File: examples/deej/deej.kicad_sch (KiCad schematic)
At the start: 27 parts, among them U1 2821, U2 5836

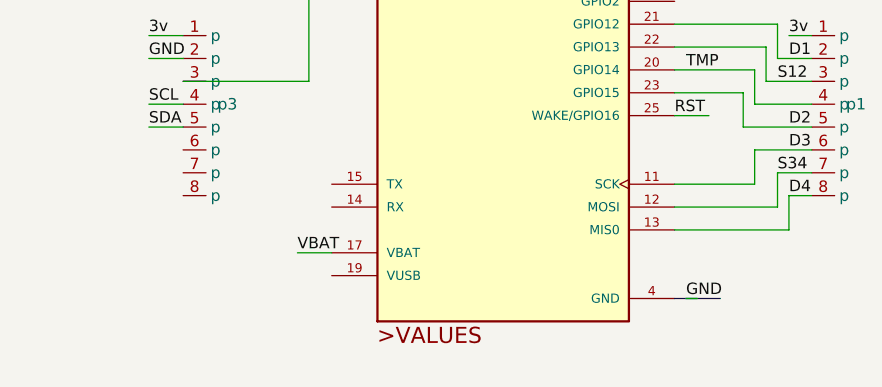
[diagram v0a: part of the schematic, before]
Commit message: updated deej example with traces for input power
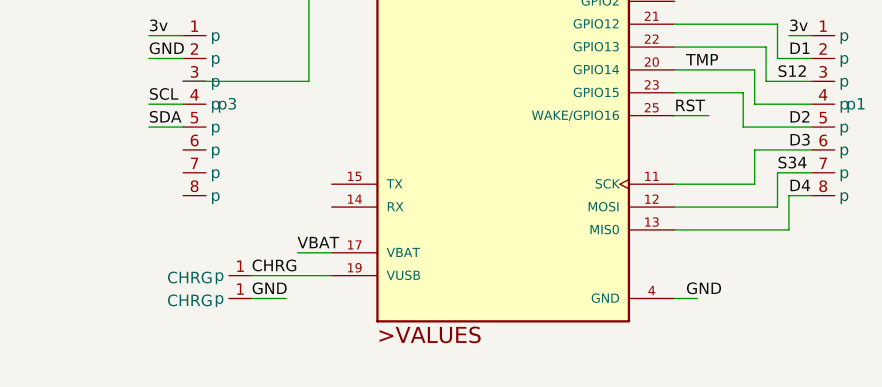
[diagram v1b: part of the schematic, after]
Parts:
- added p7, p8: CHRG, symbol Adafruit:Through_Hole_0.1in_1_Pin 4154
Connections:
- net GND: now also U1.4 (GND), p8.1 (p)
- net CHRG: now reaches U1.19 (VUSB)
- net CHRG: now also p7.1 (p)
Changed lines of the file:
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@@
+	(wire
+		(pts
+			(xy 129.54 124.46) (xy 133.35 124.46)
+		)
+		(stroke
+			(width 0)
+			(type default)
+		)
+	)
 	(wire
 		(pts
@@
 	(wire
 		(pts
+			(xy 176.53 124.46) (xy 179.07 124.46)
+		)
+		(stroke
+			(width 0)
+			(type default)
+		)
+	)
+	(wire
+		(pts
 			(xy 133.35 76.2) (xy 138.43 76.2)
 		)
@@
 	(wire
 		(pts
+			(xy 129.54 121.92) (xy 138.43 121.92)
+		)
+		(stroke
+			(width 0)
+			(type default)
+		)
+	)
+	(wire
+		(pts
 			(xy 80.01 128.27) (xy 85.09 128.27)
 		)
@@
 	(wire
 		(pts
-			(xy 177.8 124.46) (xy 179.07 124.46)
-		)
-		(stroke
-			(width 0)
-			(type default)
-		)
-	)
-	(wire
-		(pts
 			(xy 53.34 87.63) (xy 57.15 87.63)
 		)
@@
 		(pts
 			(xy 118.11 102.87) (xy 121.92 102.87)
-		)
-		(stroke
-			(width 0)
-			(type default)
-		)
-	)
-	(bus
-		(pts
-			(xy 176.53 124.46) (xy 181.61 124.46)
 		)
 		(stroke
@@
 		)
 	)
+	(label "CHRG"
+		(at 129.54 121.92 0)
+		(effects
+			(font
+				(size 1.27 1.27)
+			)
+			(justify left bottom)
+		)
+	)
 	(label "GND"
 		(at 26.67 87.63 0)
@@
 	(label "D3"
 		(at 189.23 107.95 0)
+		(effects
+			(font
+				(size 1.27 1.27)
+			)
+			(justify left bottom)
+		)
+	)
+	(label "GND"
+		(at 129.54 124.46 0)
 		(effects
 			(font
@@
 	)
 	(symbol
+		(lib_id "Adafruit:Through_Hole_0.1in_1_Pin 4154")
+		(at 127 124.46 180)
+		(unit 1)
+		(exclude_from_sim no)
+		(in_bom yes)
+		(on_board yes)
+		(dnp no)
+		(property "Reference" "p8"
+			(at 128.016 125.984 0)
+			(effects
+				(font
+					(size 1.27 1.27)
+				)
+				(hide yes)
+			)
+		)
+		(property "Value" "CHRG"
+			(at 122.682 124.714 0)
+			(effects
+				(font
+					(size 1.27 1.27)
+				)
+			)
+		)
+		(property "Footprint" ""
+			(at 127 124.46 0)
+			(effects
+				(font
+					(size 1.27 1.27)
+				)
+				(hide yes)
+			)
+		)
+		(property "Datasheet" ""
+			(at 127 124.46 0)
+			(effects
+				(font
+					(size 1.27 1.27)
+				)
+				(hide yes)
+			)
+		)
+		(property "Description" ""
+			(at 127 124.46 0)
+			(effects
+				(font
+					(size 1.27 1.27)
+				)
+				(hide yes)
+			)
+		)
+		(pin "1"
+		)
+		(instances
+			(project "deej"
+				(path "/34a0193a-017c-4da7-89e8-0cf139391c49"
+					(reference "p8")
+					(unit 1)
+				)
+			)
+		)
+	)
+	(symbol
 		(lib_id "SparkFun-Resistor:R_Potentiometer_Slide35mm")
 		(at 88.9 97.79 0)
@@
 					(unit 1)
 				)
+			)
+		)
+	)
+	(symbol
+		(lib_id "Adafruit:Through_Hole_0.1in_1_Pin 4154")
+		(at 127 121.92 180)
+		(unit 1)
+		(exclude_from_sim no)
+		(in_bom yes)
+		(on_board yes)
+		(dnp no)
+		(property "Reference" "p7"
+			(at 128.016 123.444 0)
+			(effects
+				(font
+					(size 1.27 1.27)
+				)
+				(hide yes)
+			)
+		)
+		(property "Value" "CHRG"
+			(at 122.682 122.174 0)
+			(effects
+				(font
+					(size 1.27 1.27)
+				)
+			)
+		)
+		(property "Footprint" ""
+			(at 127 121.92 0)
+			(effects
+				(font
+					(size 1.27 1.27)
+				)
+				(hide yes)
+			)
+		)
+		(property "Datasheet" ""
+			(at 127 121.92 0)
+			(effects
+				(font
+					(size 1.27 1.27)
+				)
+				(hide yes)
+			)
+		)
+		(property "Description" ""
+			(at 127 121.92 0)
+			(effects
+				(font
+					(size 1.27 1.27)
+				)
+				(hide yes)
+			)
+		)
+		(pin "1"
+		)
+		(instances
+			(project ""
+				(path "/34a0193a-017c-4da7-89e8-0cf139391c49"
+					(reference "p7")
+					(unit 1)
+				)

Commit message: fix deej pcb design
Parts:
- p7, p8: footprint (none) -> Adafruit:Through Hole 0.1in 1 Pin
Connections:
- net SCL: now also p3.3 (p); no longer p3.4 (p)
- net SDA: now also p3.4 (p); no longer p3.5 (p)
- net at R6.2, R7.2, U1.5 (ADC): no longer p3.3 (p)
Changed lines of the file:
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@@
-	)
-	(junction
-		(at 135.89 85.09)
-		(diameter 0)
-		(color 0 0 0 0)
 	)
 	(junction
@@
 	(wire
 		(pts
-			(xy 118.11 105.41) (xy 121.92 105.41)
-		)
-		(stroke
-			(width 0)
-			(type default)
-		)
-	)
-	(wire
-		(pts
 			(xy 229.87 91.44) (xy 229.87 86.36)
 		)
@@
 	(wire
 		(pts
-			(xy 135.89 85.09) (xy 135.89 100.33)
-		)
-		(stroke
-			(width 0)
-			(type default)
-		)
-	)
-	(wire
-		(pts
 			(xy 186.69 100.33) (xy 191.77 100.33)
 		)
@@
 	(wire
 		(pts
-			(xy 121.92 100.33) (xy 135.89 100.33)
-		)
-		(stroke
-			(width 0)
-			(type default)
-		)
-	)
-	(wire
-		(pts
 			(xy 92.71 113.03) (xy 97.79 113.03)
 		)
@@
 	(wire
 		(pts
+			(xy 118.11 100.33) (xy 121.92 100.33)
+		)
+		(stroke
+			(width 0)
+			(type default)
+		)
+	)
+	(wire
+		(pts
 			(xy 212.09 102.87) (xy 232.41 102.87)
 		)
@@
 	(wire
 		(pts
+			(xy 118.11 102.87) (xy 121.92 102.87)
+		)
+		(stroke
+			(width 0)
+			(type default)
+		)
+	)
+	(wire
+		(pts
 			(xy 187.96 97.79) (xy 191.77 97.79)
 		)
@@
 		(pts
 			(xy 176.53 78.74) (xy 181.61 78.74)
-		)
-		(stroke
-			(width 0)
-			(type default)
-		)
-	)
-	(wire
-		(pts
-			(xy 118.11 102.87) (xy 121.92 102.87)
 		)
 		(stroke
@@
 	)
 	(label "SDA"
-		(at 118.11 105.41 0)
+		(at 118.11 102.87 0)
 		(effects
 			(font
@@
 	)
 	(label "SCL"
-		(at 118.11 102.87 0)
+		(at 118.11 100.33 0)
 		(effects
 			(font
@@
 			)
 		)
-		(property "Footprint" ""
+		(property "Footprint" "Adafruit:Through Hole 0.1in 1 Pin"
 			(at 127 124.46 0)
 			(effects
@@
 			)
 		)
-		(property "Footprint" ""
+		(property "Footprint" "Adafruit:Through Hole 0.1in 1 Pin"
 			(at 127 121.92 0)
 			(effects

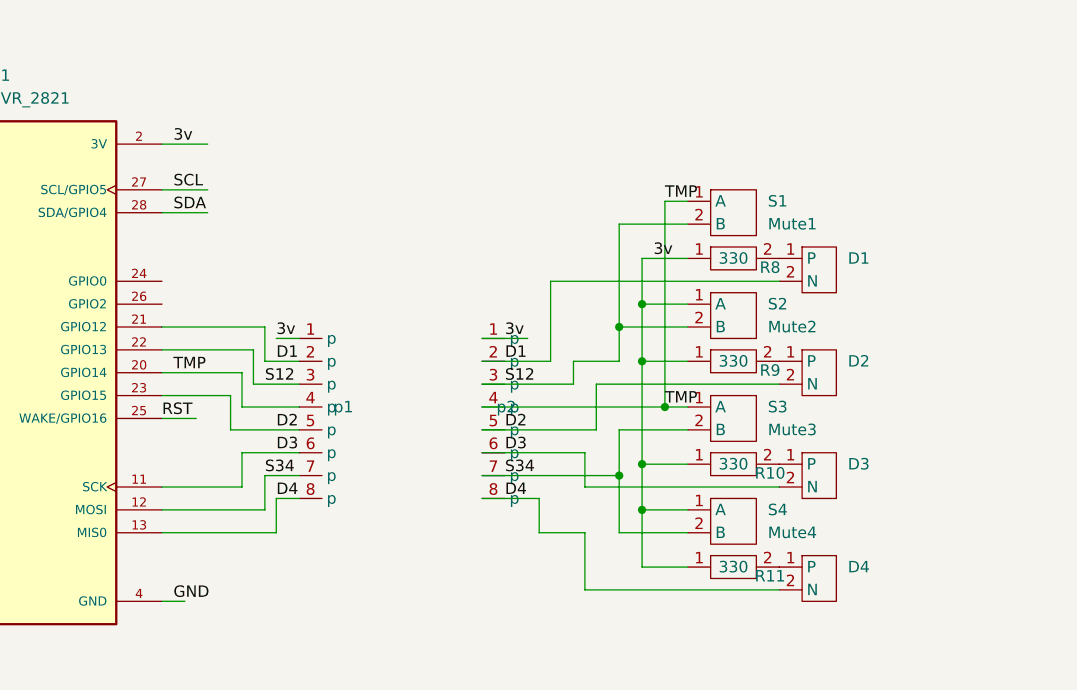
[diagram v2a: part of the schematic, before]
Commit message: add MCP23008 GPIO over I2C chip
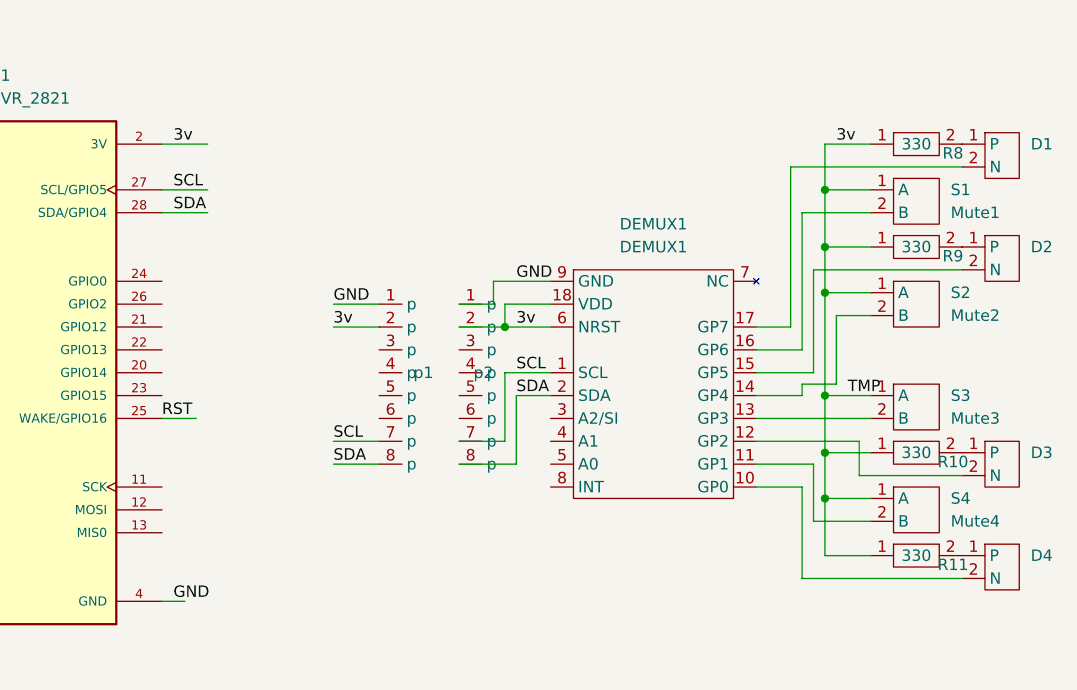
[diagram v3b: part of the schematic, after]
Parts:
- added DEMUX1: DEMUX1, Adafruit:DEMUX_MCP23008_593, symbol Adafruit:DEMUX_MCP23008_593
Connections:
- net 3v: now also S1.1 (A), S3.1 (A), p1.2 (p), p2.2 (p), DEMUX1.18 (VDD), DEMUX1.6 (NRST); no longer p1.1 (p), p2.1 (p)
- net GND: now also p1.1 (p), p2.1 (p), DEMUX1.9 (GND)
- net SCL: now also p1.7 (p), p2.7 (p), DEMUX1.1 (SCL)
- net SDA: now also p1.8 (p), p2.8 (p), DEMUX1.2 (SDA)
- removed net D1: D1.2 (N), U1.21 (GPIO12), p1.2 (p), p2.2 (p)
- removed net D2: D2.2 (N), U1.23 (GPIO15), p1.5 (p), p2.5 (p)
- removed net D3: D3.2 (N), U1.11 (SCK), p1.6 (p), p2.6 (p)
- removed net D4: D4.2 (N), U1.13 (MIS0), p1.8 (p), p2.8 (p)
- removed net S12: S1.2 (B), S2.2 (B), U1.22 (GPIO13), p1.3 (p), p2.3 (p)
- removed net S34: S3.2 (B), S4.2 (B), U1.12 (MOSI), p1.7 (p), p2.7 (p)
- removed net TMP: S1.1 (A), S3.1 (A), U1.20 (GPIO14), p1.4 (p), p2.4 (p)
- new net: DEMUX1.13 (GP3), S3.2 (B)
- new net: D3.2 (N), DEMUX1.12 (GP2)
- new net: D2.2 (N), DEMUX1.15 (GP5)
- new net: D4.2 (N), DEMUX1.10 (GP0)
- new net: DEMUX1.11 (GP1), S4.2 (B)
- new net: DEMUX1.14 (GP4), S2.2 (B)
- new net: DEMUX1.16 (GP6), S1.2 (B)
- new net: D1.2 (N), DEMUX1.17 (GP7)
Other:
- moved on the sheet: D1, D2, D3, D4, R10, R11, R8, R9, S1, S2, S3, S4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
